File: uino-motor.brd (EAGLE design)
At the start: 57.1 x 53.3 mm, 26 parts, among them IC1 TB6612FNG, J1 CON_TERMINAL_BLOCK_02-5MM, J2 CON_TERMINAL_BLOCK_02-5MM, J3 CON_TERMINAL_BLOCK_02-5MM, Q1 P-FET, U1 74*1G57, U2 74*1G57

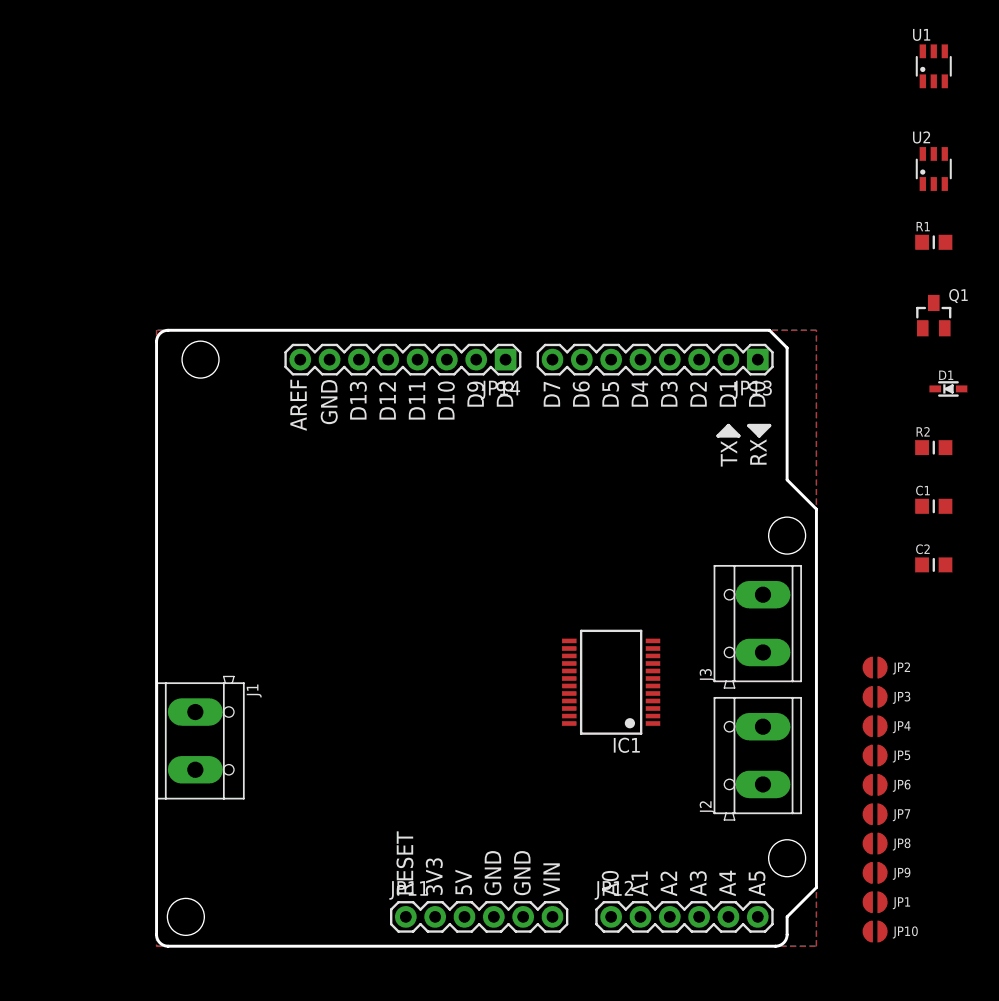
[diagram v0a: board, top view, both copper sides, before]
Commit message: Added pull-down at logic gate inputs.  Routed board.
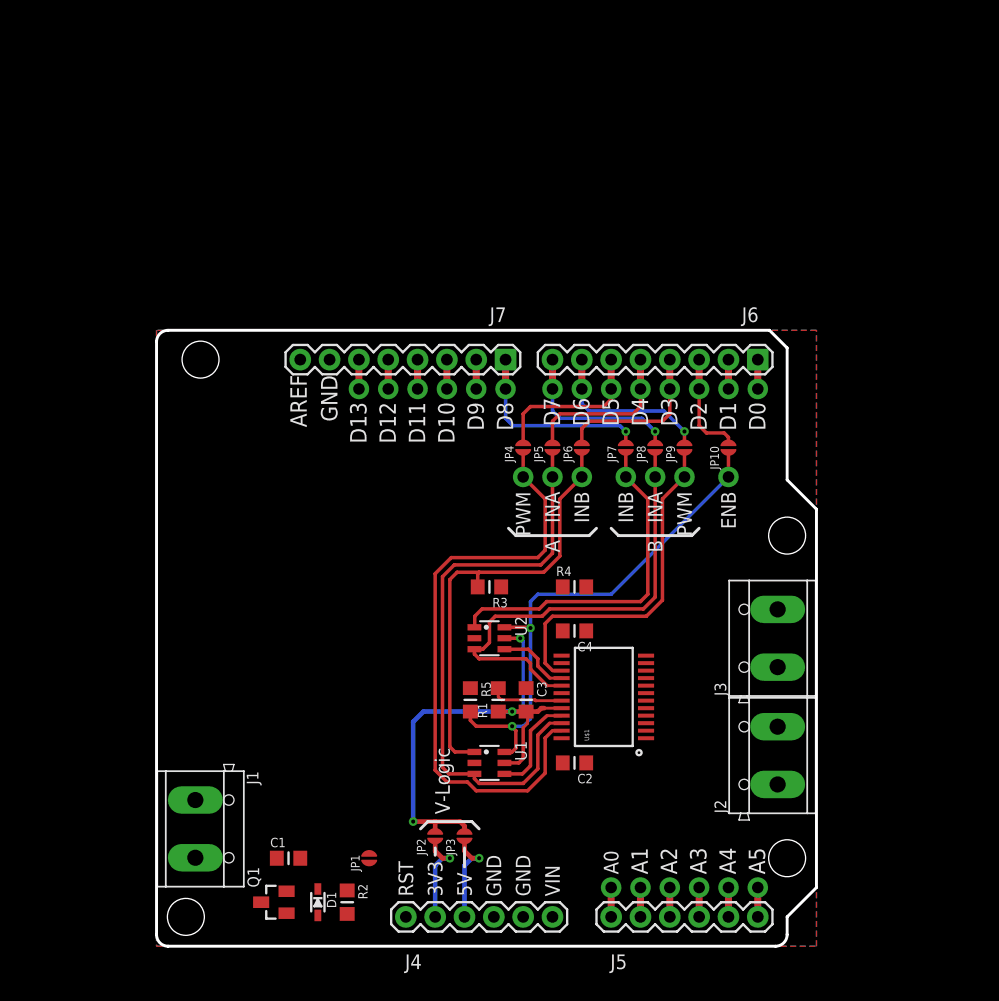
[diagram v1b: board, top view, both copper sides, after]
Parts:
- removed IC1: TB6612FNG, adafruit:SSOP24
- added C3, C4: (no value), rc-master-smd:C0805MP
- added R3, R4, R5: (no value), rc-master-smd:R0805MP
- added U$1: TB6612FNG, SparkFun-PowerIC:SSOP24
- JP1, JP10, JP2, JP3, JP4, JP5, JP6, JP7, JP8, JP9: value SJ-055 -> SJ-035; device jumpers:SJ-055 -> jumpers:SJ-035
- moved Q1 76.5 mm to (21.6, 3.81), turned to 90 degrees
- moved U1 71.6 mm to (40.3, 15.9), turned to 270 degrees
- moved D1 70.4 mm to (25.4, 3.81), turned to 270 degrees
- moved R2 64.3 mm to (27.9, 3.81), turned to 270 degrees
- moved C1 63.7 mm to (22.9, 7.62)
- moved U2 56.0 mm to (40.3, 26.7), turned to 270 degrees
- moved R1 54.7 mm to (41.0, 21.3), turned to 90 degrees
- moved JP1 44.0 mm to (29.8, 7.62), turned to 270 degrees
- moved JP10 43.8 mm to (61.0, 43.2), turned to 90 degrees
- moved JP2 40.8 mm to (35.6, 9.53), turned to 270 degrees
- moved JP9 40.4 mm to (57.1, 43.2), turned to 90 degrees
- moved JP8 39.2 mm to (54.6, 43.2), turned to 90 degrees
- moved JP4 38.9 mm to (43.2, 43.2), turned to 90 degrees
- moved JP6 38.7 mm to (48.3, 43.2), turned to 90 degrees
- moved JP5 38.6 mm to (45.7, 43.2), turned to 90 degrees
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- renumbered JP11 to J4, JP12 to J5, JP13 to J6, JP14 to J7
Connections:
- removed net ACTRL: JP6.1, U1.1
- removed net ADIR: IC1.21, JP5.1, U1.3
- removed net AIN2: IC1.22, U1.4
- removed net APWM: IC1.23, JP4.1
- removed net BCTRL: JP9.1, U2.1
- removed net BDIR: IC1.17, JP8.1, U2.3
- removed net BPWM: IC1.15, JP7.1
- removed net EN: JP10.1, U1.6, U2.6
- removed net N$2: IC1.5, IC1.6, J2.1
- removed net N$3: IC1.7, IC1.8, J3.2
- removed net N$4: IC1.11, IC1.12, J3.1
- removed net N$5: IC1.19, R1.2
- new net A-INA: JP5.1, U$1.22, U1.3
- new net A-INB: JP6.1, R3.2, U1.1
- new net A-PWM: JP4.1, U$1.23
- new net AIN1: U$1.21, U1.4
- new net B-INA: JP8.1, U$1.17, U2.3
- new net B-INB: JP7.1, R4.2, U2.1
- new net B-PWM: JP9.1, U$1.15
- new net ENB: JP10.1, R5.2, U1.6, U2.6
- new net N$10: J2.2, U$1.1, U$1.2
- new net N$11: J3.1, U$1.11, U$1.12
- new net N$12: J2.1, U$1.5, U$1.6
- new net N$13: J3.2, U$1.7, U$1.8
- net BIN2: now also U$1.16; no longer IC1.16
- net D10: no longer JP7.2
- net D2: now also JP10.2
- net D3: now also JP6.2
- net D4: now also JP5.2
- net D5: now also JP4.2; no longer JP10.2, JP6.2
- net D7: now also JP8.2; no longer JP5.2
- net D8: now also JP7.2; no longer JP8.2
- net D9: no longer JP4.2
- net GND: now also C3.1, C4.1, R3.1, R4.1, R5.1, U$1.10, U$1.18, U$1.3, U$1.4, U$1.9; no longer IC1.10, IC1.18, IC1.3, IC1.4, IC1.9
- net N$1: now also R1.2, U$1.19; no longer IC1.1, IC1.2, J2.2
- net VCC: now also C3.2, U$1.20; no longer IC1.20
- net VDD: now also C4.2, U$1.13, U$1.14, U$1.24; no longer IC1.13, IC1.14, IC1.24
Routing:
- net A-PWM: track 0.00 -> 52.3 mm, vias 0 -> 1
- net A-INA: track 0.00 -> 50.6 mm, vias 0 -> 1
- net ENB: track 0.00 -> 45.8 mm, vias 0 -> 3
- net VCC: track 0.00 -> 43.8 mm, vias 0 -> 3
- net B-INA: track 0.00 -> 40.5 mm, vias 0 -> 1
- net A-INB: track 0.00 -> 38.3 mm, vias 0 -> 1
- net B-INB: track 0.00 -> 29.9 mm, vias 0 -> 1
- net B-PWM: track 0.00 -> 29.7 mm, vias 0 -> 1
- net D8: track 0.00 -> 17.0 mm, vias 0 -> 2
- net D7: track 0.00 -> 15.1 mm, vias 0 -> 2
- net D6: track 0.00 -> 14.7 mm, vias 0 -> 2
- net D4: track 0.00 -> 14.1 mm, vias 0 -> 1
- net D3: track 0.00 -> 14.1 mm, vias 0 -> 1
- net D5: track 0.00 -> 14.1 mm, vias 0 -> 1
- net D2: track 0.00 -> 9.18 mm, vias 0 -> 1
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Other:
- board text added: "A"
- board text added: "B"
- board text added: "ENB"
- board text added: "INA"
- board text added: "INB"
- board text added: "PWM"
- board text added: "RST"
- board text added: "V-Logic"
- board text removed: "RESET"
- board text removed: "RX"
- board text removed: "TX"

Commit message: Parts placed and major routing completed.
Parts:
- added F1: (no value), adi-misc:PTC
- moved Q1 7.96 mm to (25.4, 10.8)
- moved D1 7.67 mm to (28.6, 10.8)
- moved C1 6.98 mm to (29.8, 7.62)
- moved R2 4.58 mm to (25.4, 7.62), turned to 180 degrees
- moved JP1 2.68 mm to (30.1, 4.95)
- moved C2 2.54 mm to (50.2, 15.9)
- moved C4 2.54 mm to (50.2, 27.3)
- moved R4 2.54 mm to (50.2, 31.1)
- moved JP2 2.16 mm to (35.6, 11.7)
- moved JP3 2.16 mm to (38.1, 11.7)
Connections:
- net N$10 renamed A01
- net N$11 renamed B01
- net N$12 renamed A02
- net N$13 renamed B02
- removed net N$8: J1.1, Q1.3
- new net N$5: F1.P$1, J1.1
- new net N$7: F1.P$2, Q1.3
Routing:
- net N$7: track 0.00 -> 24.1 mm, vias 0 -> 2
- net N$5: track 0.00 -> 17.3 mm
- net VIN: track 0.00 -> 16.8 mm
- net N$6: track 0.00 -> 5.94 mm
- net VCC: track 43.8 -> 39.8 mm
- net GND: track 0.00 -> 3.26 mm
- net VDD: track 0.00 -> 1.44 mm
- net B-INB: track 29.9 -> 31.1 mm
- net 5V: track 8.40 -> 9.29 mm
- net 3V3: track 8.40 -> 9.29 mm
- added copper zone on layer 1, net A01
- added copper zone on layer 1, net A02
- added copper zone on layer 1, net B01
- added copper zone on layer 1, net B02
- added copper zone on layer 1, net VDD

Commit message: Added values. Version 0.1
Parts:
- removed U$1: TB6612FNG, SparkFun-PowerIC:SSOP24
- added U3: TB6612FNG, SparkFun-PowerIC:SSOP24
- C1, C2, C3: value (none) -> 10u
- C4: value (none) -> 10y
- R1, R2, R3, R4, R5: value (none) -> 100k
- moved J2 11.6 mm to (53.2, 16.5)
- moved J3 11.6 mm to (53.2, 26.7)
- moved J4 11.4 mm to (21.6, 2.54)
- moved JP2 11.4 mm to (24.1, 11.7)
- moved C1 11.4 mm to (18.4, 7.62)
- moved C2 11.4 mm to (38.7, 15.9)
- moved C3 11.4 mm to (32.0, 21.3)
- moved C4 11.4 mm to (38.7, 27.3)
- moved D1 11.4 mm to (17.1, 10.8)
- moved F1 11.4 mm to (12.7, 3.17)
- moved J5 11.4 mm to (39.4, 2.54)
- moved J6 11.4 mm to (52.1, 50.8)
- moved J7 11.4 mm to (30.2, 50.8)
- moved JP1 11.4 mm to (18.7, 4.95)
- moved JP10 11.4 mm to (49.5, 43.2)
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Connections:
- net A-INA: now also U3.22; no longer U$1.22
- net A-PWM: now also U3.23; no longer U$1.23
- net A01: now also U3.1, U3.2; no longer U$1.1, U$1.2
- net A02: now also U3.5, U3.6; no longer U$1.5, U$1.6
- net AIN1: now also U3.21; no longer U$1.21
- net B-INA: now also U3.17; no longer U$1.17
- net B-PWM: now also U3.15; no longer U$1.15
- net B01: now also U3.11, U3.12; no longer U$1.11, U$1.12
- net B02: now also U3.7, U3.8; no longer U$1.7, U$1.8
- net BIN2: now also U3.16; no longer U$1.16
- net GND: now also U3.10, U3.18, U3.3, U3.4, U3.9; no longer U$1.10, U$1.18, U$1.3, U$1.4, U$1.9
- net N$1: now also U3.19; no longer U$1.19
- net VCC: now also U3.20; no longer U$1.20
- net VDD: now also U3.13, U3.14, U3.24; no longer U$1.13, U$1.14, U$1.24
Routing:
- net A5: track 2.54 -> 5.08 mm
- net A4: track 2.54 -> 5.08 mm
- net A3: track 2.54 -> 5.08 mm
- net A2: track 2.54 -> 5.08 mm
- net A1: track 2.54 -> 5.08 mm
- net A0: track 2.54 -> 5.08 mm
- net D9: track 2.54 -> 5.08 mm
- net D8: track 17.0 -> 19.5 mm
- net D7: track 15.1 -> 17.6 mm
- net D5: track 14.1 -> 16.7 mm
- net D3: track 14.1 -> 16.7 mm
- net D13: track 2.54 -> 5.08 mm
- net D12: track 2.54 -> 5.08 mm
- net D11: track 2.54 -> 5.08 mm
- net D10: track 2.54 -> 5.08 mm
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- added copper zone on layer 16, net A01
- added copper zone on layer 16, net A02
- added copper zone on layer 16, net B01
- added copper zone on layer 16, net B02
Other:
- board text added: "*uino-motor"
- board text added: "by Adi Linden"
- board text added: "v0.1 2016/11/12"
